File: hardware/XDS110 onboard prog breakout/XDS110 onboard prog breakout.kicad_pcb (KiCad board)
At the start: 2 copper layers, 57.5 x 38.3 mm, 27 parts, among them J1 Conn_01x09_Socket, J2 Conn_01x09_Socket, Q1 2N7002, Q2 2N7002, Q3 2N7002, Q4 2N7002, Q5 2N7002, Q6 2N7002

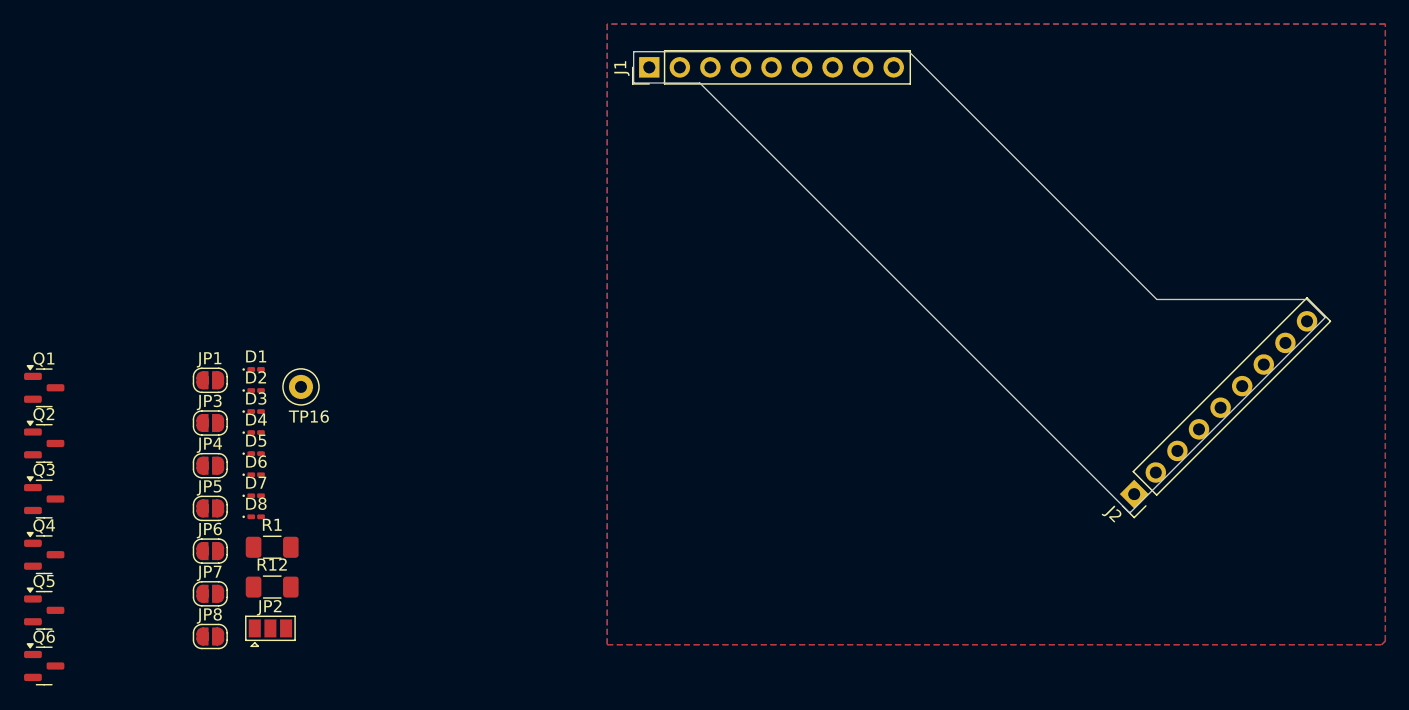
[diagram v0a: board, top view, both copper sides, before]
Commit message: complete breakout board
used auto router. doubt signal integrity will be a problem. power delivery maybe, the traces are kinda small
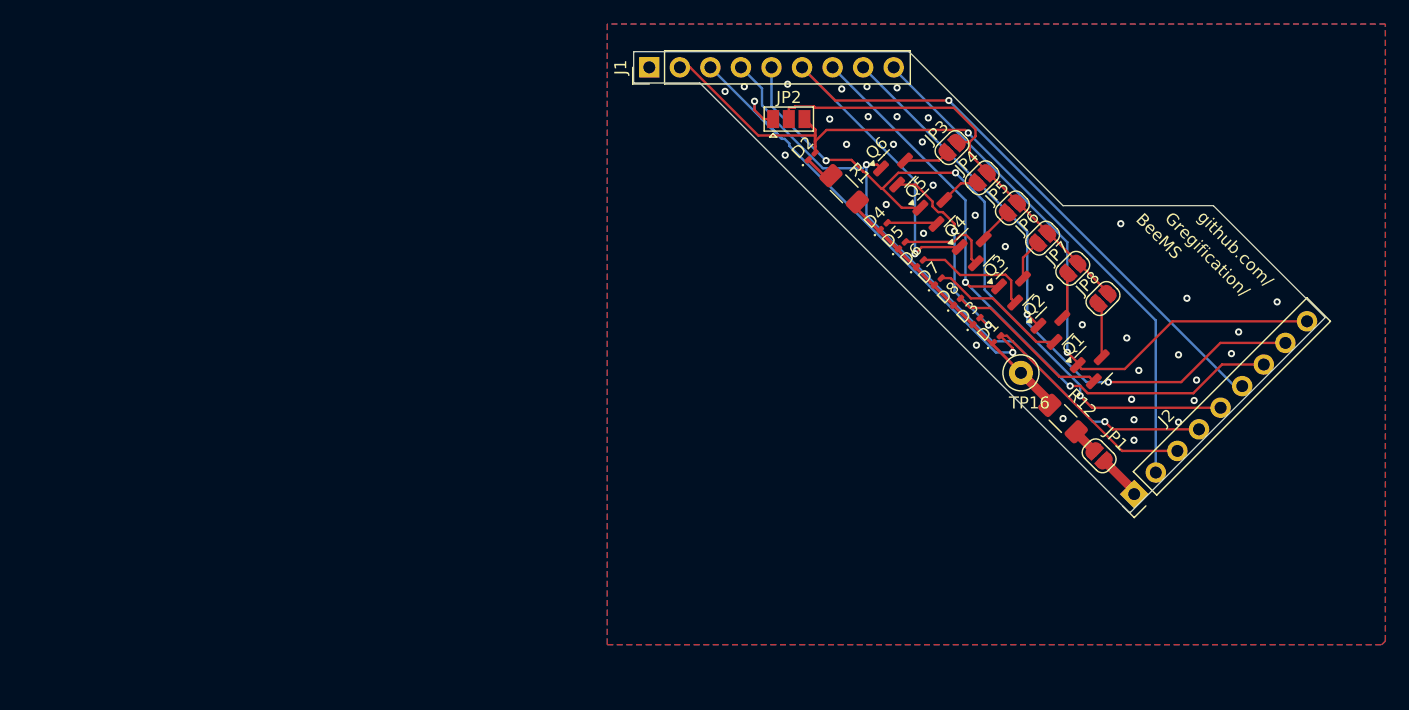
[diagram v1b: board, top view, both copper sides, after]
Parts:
- moved Q1 87.3 mm to (123.8, 119.3), turned to 45 degrees
- moved Q2 84.6 mm to (120.5, 116.0), turned to 45 degrees
- moved Q3 82.6 mm to (117.2, 112.7), turned to 45 degrees
- moved Q6 82.1 mm to (107.4, 102.9), turned to 45 degrees
- moved Q4 81.6 mm to (113.9, 109.5), turned to 45 degrees
- moved Q5 81.4 mm to (110.7, 106.2), turned to 45 degrees
- moved JP8 79.4 mm to (124.5, 113.7), turned to 45 degrees
- moved JP7 76.6 mm to (122.0, 111.2), turned to 45 degrees
- moved JP1 74.2 mm to (124.2, 126.8), turned to 135 degrees
- moved JP6 73.9 mm to (119.5, 108.7), turned to 45 degrees
- moved JP5 71.2 mm to (117.0, 106.2), turned to 45 degrees
- moved JP4 68.5 mm to (114.5, 103.7), turned to 45 degrees
- moved R12 67.2 mm to (121.2, 123.7), turned to 135 degrees
- moved JP3 65.8 mm to (112.0, 101.2), turned to 45 degrees
- moved D1 61.6 mm to (115.7, 117.1), turned to 45 degrees
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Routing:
- net /XDS_RESET_OUT: track 0.00 -> 70.9 mm, vias 0 -> 2
- net /XDS_5v_supply: track 0.00 -> 65.2 mm, vias 0 -> 1
- net /XDS_3v_supply: track 0.00 -> 60.8 mm, vias 0 -> 2
- net /XDS_RXD: track 0.00 -> 60.7 mm, vias 0 -> 3
- net /XDS_TXD: track 0.00 -> 55.5 mm, vias 0 -> 2
- net /XDS_TMS_SWDIO: track 0.00 -> 55.0 mm, vias 0 -> 2
- net /XDS_TCK_SWDCLK: track 0.00 -> 53.1 mm, vias 0 -> 2
- net /XDS_BLS_INVOKE: track 0.00 -> 51.9 mm, vias 0 -> 1
- net Net-(JP2-C): track 0.00 -> 37.0 mm
- net Net-(D1-K): track 0.00 -> 26.9 mm
- net Net-(D3-A): track 0.00 -> 16.9 mm, vias 0 -> 2
- net Net-(D8-A): track 0.00 -> 13.9 mm
- net Net-(D7-A): track 0.00 -> 11.6 mm
- net Net-(D6-A): track 0.00 -> 10.0 mm
- net Net-(D5-A): track 0.00 -> 7.97 mm
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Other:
- outline, holes or cut-outs redrawn
- board text added: "BeeMS"
- board text added: "Gregification/"
- board text added: "XDS110 jumper. cheesed routing. not for high speed or power"
- board text added: "github.com/"

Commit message: complete layout
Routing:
- net /XDS_GND: vias 37 -> 40
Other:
- outline, holes or cut-outs redrawn
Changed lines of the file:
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@@
 		(pts
 			(xy 85.5 93.2) (xy 108.4 93.2) (xy 121.2 106) (xy 133.7 106) (xy 143 115.3) (xy 126.8 131.5) (xy 126.7 131.5)
-			(xy 91 95.8) (xy 85.5 95.8)
+			(xy 92 96.8) (xy 85.5 96.8)
 		)
 		(stroke
@@
 	)
 	(via
+		(at 105.1 96.2)
+		(size 0.6)
+		(drill 0.3)
+		(layers "F.Cu" "B.Cu")
+		(free yes)
+		(net 17)
+	)
+	(via
 		(at 139 114)
 		(size 0.6)
@@
 	)
 	(via
-		(at 107.4 98.6)
-		(size 0.6)
-		(drill 0.3)
-		(layers "F.Cu" "B.Cu")
-		(free yes)
-		(net 17)
-	)
-	(via
 		(at 109.5 100.7)
 		(size 0.6)
@@
 	)
 	(via
-		(at 105 98.6)
-		(size 0.6)
-		(drill 0.3)
-		(layers "F.Cu" "B.Cu")
-		(free yes)
-		(net 17)
-	)
-	(via
 		(at 135.8 116.5)
 		(size 0.6)
@@
 	)
 	(via
+		(at 107.4 98.7)
+		(size 0.6)
+		(drill 0.3)
+		(layers "F.Cu" "B.Cu")
+		(free yes)
+		(net 17)
+	)
+	(via
 		(at 122.8 115.9)
 		(size 0.6)
@@
 	)
 	(via
+		(at 112.2 98.7)
+		(size 0.6)
+		(drill 0.3)
+		(layers "F.Cu" "B.Cu")
+		(free yes)
+		(net 17)
+	)
+	(via
 		(at 102.8 96.3)
 		(size 0.6)
@@
 	)
 	(via
+		(at 110 96.2)
+		(size 0.6)
+		(drill 0.3)
+		(layers "F.Cu" "B.Cu")
+		(free yes)
+		(net 17)
+	)
+	(via
 		(at 132.3 120.5)
 		(size 0.6)
@@
 	)
 	(via
+		(at 88.6 95.9)
+		(size 0.6)
+		(drill 0.3)
+		(layers "F.Cu" "B.Cu")
+		(free yes)
+		(net 17)
+	)
+	(via
 		(at 103.2 100.9)
 		(size 0.6)
@@
 	)
 	(via
-		(at 104.9 96.1)
-		(size 0.6)
-		(drill 0.3)
-		(layers "F.Cu" "B.Cu")
-		(free yes)
-		(net 17)
-	)
-	(via
 		(at 107.1 100.9)
 		(size 0.6)
@@
 		(size 0.6)
 		(drill 0.3)
+		(layers "F.Cu" "B.Cu")
+		(free yes)
+		(net 17)
+	)
+	(via
+		(at 105.1 98.7)
+		(size 0.6)
+		(drill 0.3)

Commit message: boards finalized
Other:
- board text added: "XDS110 jumper & indicators"
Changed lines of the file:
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@@
 		(layer "Edge.Cuts")
+	)
+	(gr_text "XDS110 jumper &\nindicators "
+		(at 124.35 110.1 315)
+		(layer "F.SilkS")
+		(effects
+			(font
+				(size 1 1)
+				(thickness 0.1)
+			)
+			(justify left bottom)
+		)
 	)
 	(gr_text "BeeMS"
@@
 	)
 	(segment
+		(start 134.3 122.8)
+		(end 123.75 122.9)
+		(width 0.2)
+		(layer "F.Cu")
+		(net 15)
+	)
+	(segment
 		(start 112.2603 103.2661)
 		(end 107.5005 103.2661)
@@
 	)
 	(segment
+		(start 123.75 122.9)
+		(end 122.6219 121.8102)
+		(width 0.2)
+		(layer "F.Cu")
+		(net 15)
+	)
+	(segment
 		(start 106.0874 104.5763)
 		(end 106.1903 104.5763)
@@
 		(start 107.7883 106.1742)
 		(end 106.1904 104.5762)
-		(width 0.2)
-		(layer "F.Cu")
-		(net 15)
-	)
-	(segment
-		(start 123.6117 122.8)
-		(end 122.6219 121.8102)
-		(width 0.2)
-		(layer "F.Cu")
-		(net 15)
-	)
-	(segment
-		(start 134.3 122.8)
-		(end 123.6117 122.8)
 		(width 0.2)
 		(layer "F.Cu")
@@
 	)
 	(via
-		(at 132.1 122.2)
+		(at 132.75 122.05)
 		(size 0.6)
 		(drill 0.3)
@@
 	)
 	(via
-		(at 132.3 120.5)
+		(at 132.2 120.45)
 		(size 0.6)
 		(drill 0.3)
@@
 	)
 	(via
-		(at 126.9 122.1)
+		(at 124.6 122.25)
 		(size 0.6)
 		(drill 0.3)
@@
 	)
 	(via
-		(at 130.8 124)
-		(size 0.6)
-		(drill 0.3)
+		(at 130.5 123.8)
+		(size 0.6)
+		(drill 0.3)
